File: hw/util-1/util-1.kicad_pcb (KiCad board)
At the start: 2 copper layers, 50 x 80 mm, 44 parts, among them J1 Conn_01x02, J2 Conn_01x03, J3 Conn_01x02, J4 Conn_01x02, J5 Conn_01x06, J6 Conn_01x02, J7 5V, J8 3.3V, J9 BATT, U2 NCP1117-5.0_SOT223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

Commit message: Ready to sent to fab
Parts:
- added C13: 0.1uF, Capacitor_SMD:C_0805_2012Metric_Pad1.18x1.45mm_HandSolder, F.Cu at (121.5, 128.5)
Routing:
- net +BATT: track 91.5 -> 95.7 mm
- net GND: vias 25 -> 31

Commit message: Added changes to mic preamp ground plane
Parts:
- moved J3 16.5 mm to (144.5, 95.5)
- moved C11 5.00 mm to (137.0, 95.5), turned to 180 degrees
- moved R9 5.00 mm to (137.0, 93.0)
- moved C12 4.46 mm to (136.0, 99.0)
- moved J6 3.00 mm to (144.5, 85.2)
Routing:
- net GNDA: track 61.6 -> 9.98 mm, vias 2 -> 0
- net AI_OUT: track 41.9 -> 27.5 mm
- net GND: track 3.56 -> 5.80 mm, vias 31 -> 25
- net Net-(C11-Pad2): track 2.52 -> 3.34 mm
- added copper zone on F.Cu, net GNDA

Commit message: Sending to OSHPark
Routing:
- net GNDA: track 9.98 -> 18.3 mm, vias 0 -> 2
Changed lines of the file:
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@@
 		(tags "capacitor handsolder")
 		(property "Reference" "C11"
-			(at -3.5375 0 360)
+			(at -3.5375 0 0)
 			(layer "F.SilkS")
 			(effects
@@
 		)
 		(property "Value" "10uF"
-			(at 0 1.68 360)
+			(at 0 1.68 0)
 			(layer "F.Fab")
 			(effects
@@
 		)
 		(fp_text user "${REFERENCE}"
-			(at 0 0 360)
+			(at 0 0 0)
 			(layer "F.Fab")
 			(effects
@@
 	)
 	(gr_text "MIC+"
-		(at 147 85.5 0)
+		(at 147 86 0)
 		(layer "F.SilkS")
 		(effects
@@
 		(net 13)
 	)
+	(via
+		(at 134 90.5)
+		(size 0.6)
+		(drill 0.3)
+		(layers "F.Cu" "B.Cu")
+		(free yes)
+		(net 13)
+	)
+	(via
+		(at 126.5 92.5)
+		(size 0.6)
+		(drill 0.3)
+		(layers "F.Cu" "B.Cu")
+		(free yes)
+		(net 13)
+	)
+	(segment
+		(start 126.5 92.5)
+		(end 132 92.5)
+		(width 0.2)
+		(layer "B.Cu")
+		(net 13)
+	)
+	(segment
+		(start 132 92.5)
+		(end 134 90.5)
+		(width 0.2)
+		(layer "B.Cu")
+		(net 13)
+	)

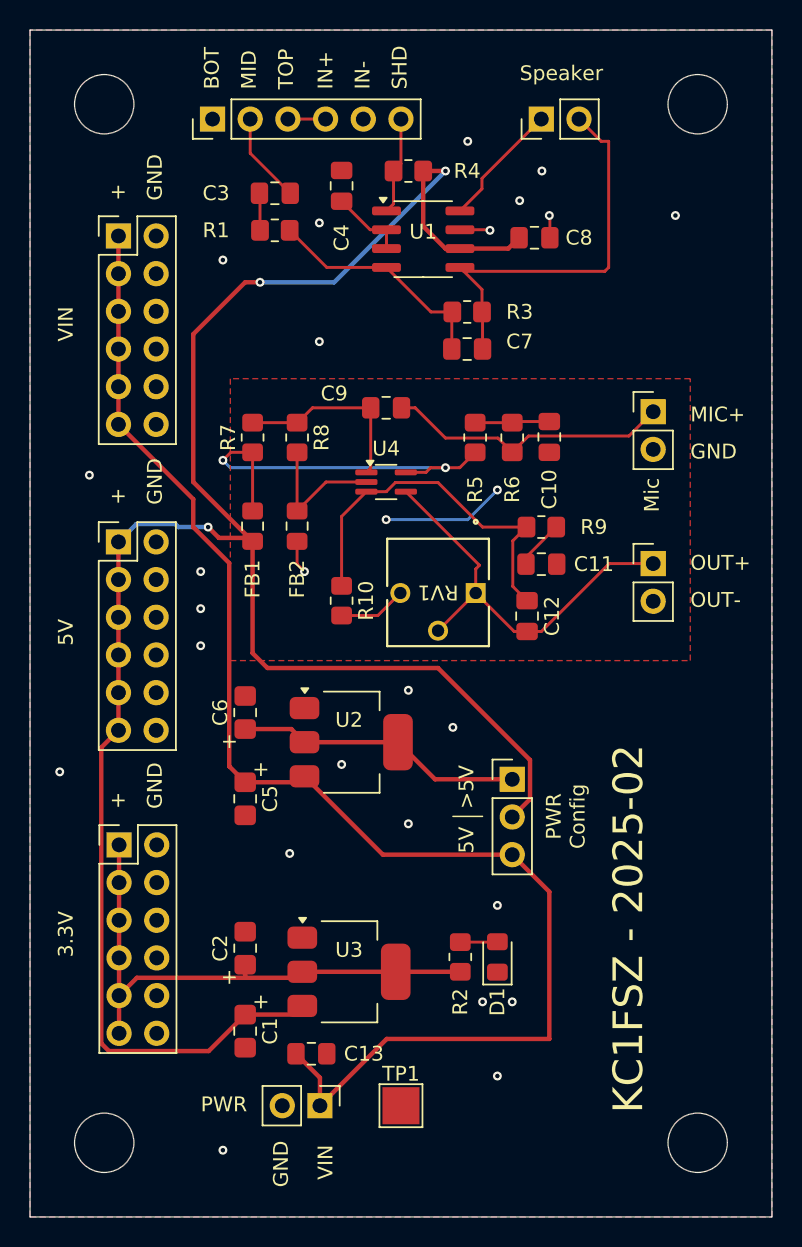
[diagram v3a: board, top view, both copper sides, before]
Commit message: Sending revision of util-1 to JLCPCB
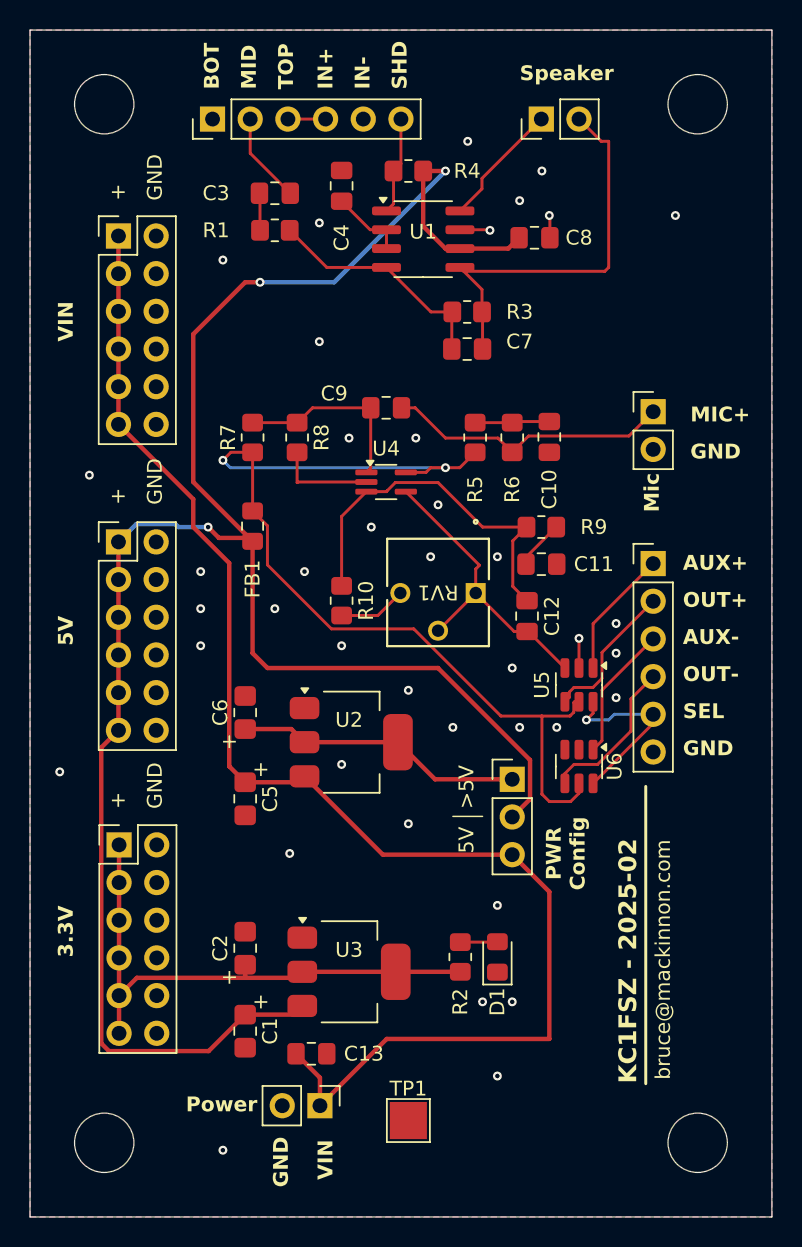
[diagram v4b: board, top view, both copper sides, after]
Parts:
- removed FB2: FerriteBead, Inductor_SMD:L_0805_2012Metric_Pad1.15x1.40mm_HandSolder
- added U5: TS5A3159ADBVR, Package_TO_SOT_SMD:SOT-23-6, F.Cu at (139.5, 103.6)
- added U6: TS5A3159ADBVR, Package_TO_SOT_SMD:SOT-23-6, F.Cu at (139.5, 109.1)
- J3: value Conn_01x02 -> Conn_01x06; footprint Connector_PinHeader_2.54mm:PinHeader_1x02_P2.54mm_Vertical -> Connector_PinHeader_2.54mm:PinHeader_1x06_P2.54mm_Vertical
- moved TP1 1.12 mm to (128.0, 133.0)
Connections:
- C10 pad 1: GNDA -> GND
- C11 pad 1: GNDA -> GND
- J3 pad 1: AI_OUT -> AUX+
- J3 pad 2: GNDA -> OUT+
- J6 pad 2: GNDA -> GND
- R8 pad 2: GNDA -> GND
- U4 pad 2: GNDA -> GND
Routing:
- net +5VA: track 26.6 -> 65.5 mm
- net GNDA: track 18.3 -> 0.00 mm, vias 2 -> 0
- net AUX_SEL: track 0.00 -> 12.6 mm, vias 0 -> 1
- net OUT-: track 0.00 -> 10.6 mm
- net OUT+: track 0.00 -> 10.3 mm
- net AUX-: track 0.00 -> 9.14 mm
- net AUX+: track 0.00 -> 8.72 mm
- net GND: track 5.80 -> 12.8 mm, vias 25 -> 40
- net AI_OUT: track 27.5 -> 20.7 mm
- removed copper zone on F.Cu, net GNDA
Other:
- board text added: "AUX+"
- board text added: "AUX-"
- board text added: "Power"
- board text added: "SEL"
- board text added: "bruce@mackinnon.com"
- board text removed: "PWR"
